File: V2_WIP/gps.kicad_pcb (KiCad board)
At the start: 6 copper layers, 82.5 x 82.5 mm, 126 parts, among them J301 USB_B_Micro, J601 BATT, P1 USB_C_Plug_USB2.0, Q1 IRLML5203, Q2 S8050, Q3 S8050, SW3 SW_Push, SW4 SW_Push, SW601 MSN22AFW01, SW701 RotaryEncoder, U1 ESP32-WROOM-32E, U10 24C32, U102 W25Q128JFV, U11 SN74LV1T34DBVRG4, U12 RT9742AGJ5F, U14 CH340K, U2 TPS613222ADBVR, U301 USBLC6-2SC6, U4 HT16k33, U401 NEO-M9N, U402 KW4-804CGB, U5 7seg_1x1_rgb, U6 7seg_1x1_rgb, U601 IP5306, U602 STC3100IST, U7 7seg_1x1_rgb, U9 TCA39306DDFR

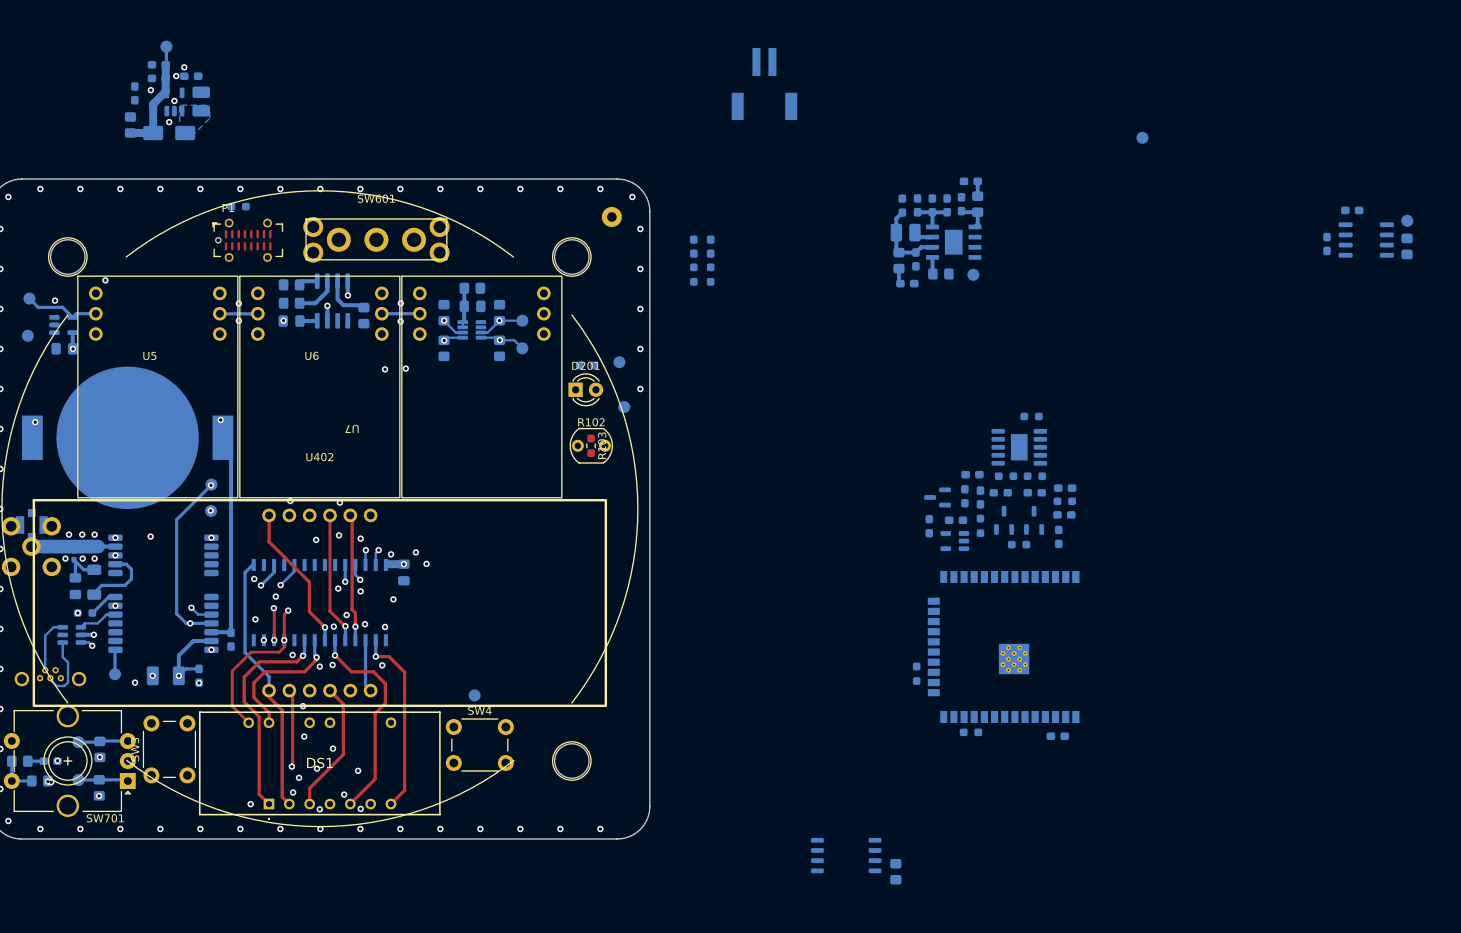
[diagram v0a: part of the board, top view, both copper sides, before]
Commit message: added USB, button
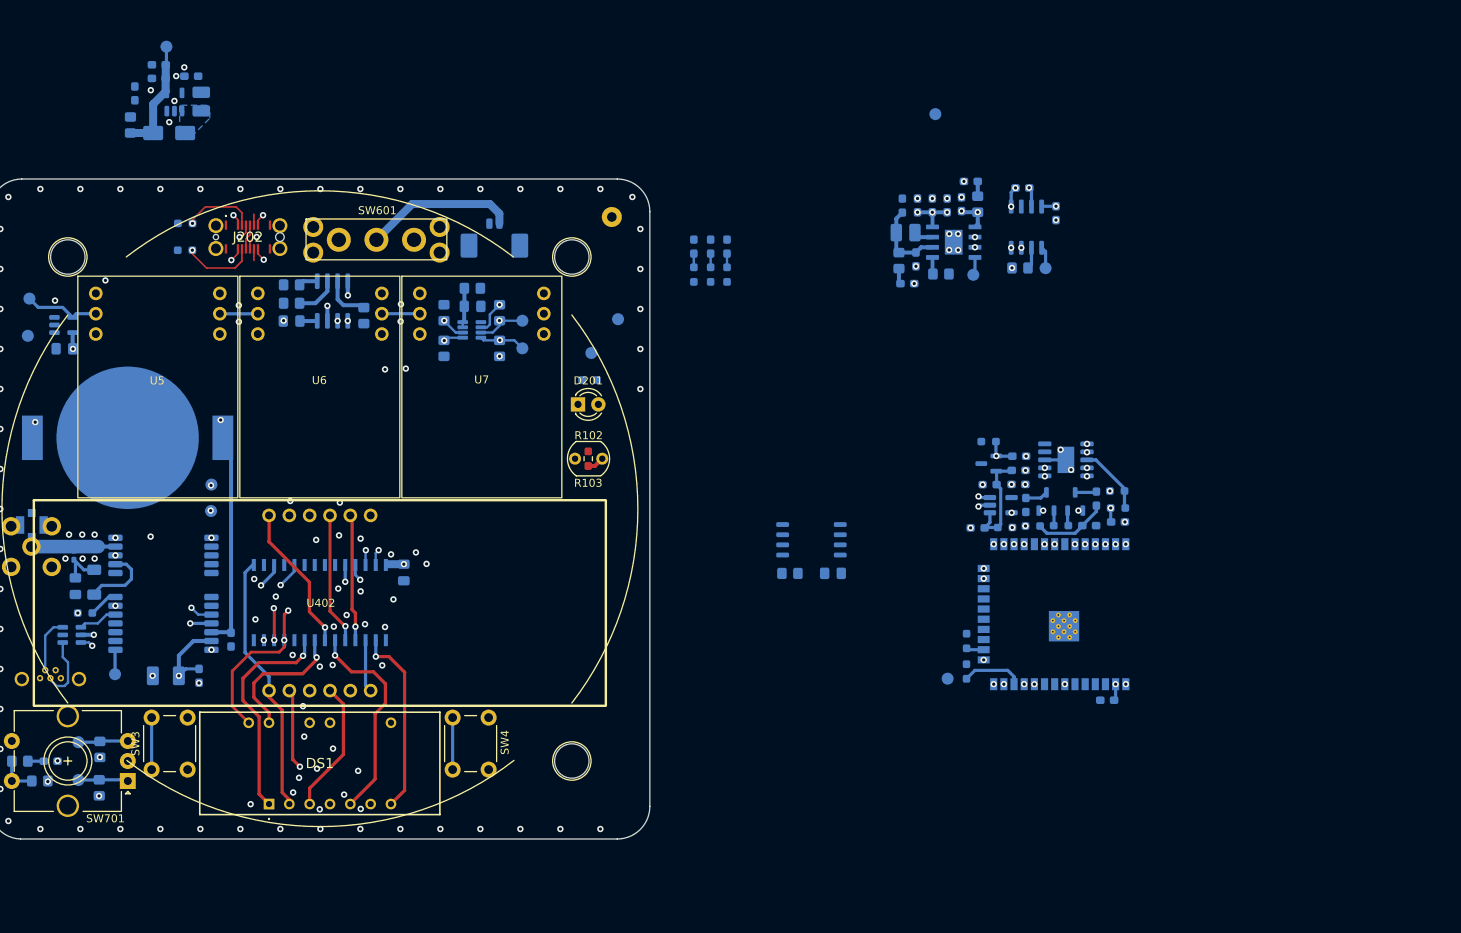
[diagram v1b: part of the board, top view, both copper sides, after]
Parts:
- removed D1: LED, Diode_SMD:D_0603_1608Metric_Pad1.05x0.95mm_HandSolder
- removed P1: USB_C_Plug_USB2.0, Connector_USB:USB_C_Receptacle_G-Switch_GT-USB-7051x
- removed R21: 5k1, Resistor_SMD:R_0603_1608Metric_Pad0.98x0.95mm_HandSolder
- removed U12: RT9742AGJ5F, Package_TO_SOT_SMD:TSOT-23-5
- added C101: 100nF, Capacitor_SMD:C_0805_2012Metric_Pad1.18x1.45mm_HandSolder, B.Cu at (158.1, 91.0)
- added D103: VUSB, Diode_SMD:D_0603_1608Metric_Pad1.05x0.95mm_HandSolder, B.Cu at (144.9, 50.2)
- added J202: USB4145-03-0230-C, KiCad:USB4145030230C, F.Cu at (85.0, 49.0)
- added R104: 2k, Resistor_SMD:R_0603_1608Metric_Pad0.98x0.95mm_HandSolder, B.Cu at (144.9, 53.7)
- added R204: 5k1, Resistor_SMD:R_0603_1608Metric_Pad0.98x0.95mm_HandSolder, B.Cu at (77.2, 47.3)
- added R205: 5k1, Resistor_SMD:R_0603_1608Metric_Pad0.98x0.95mm_HandSolder, B.Cu at (77.2, 50.6)
- added U201: RT9080, Package_TO_SOT_SMD:SOT-23-5_HandSoldering, B.Cu at (179.1, 82.5)
- D101: value LED -> +3V3
- D102: value LED -> +5V
- J601: footprint 1769:1769 -> Connector_Molex:Molex_PicoBlade_53398-0271_1x02-1MP_P1.25mm_Vertical
- SW3, SW4: value SW_Push -> FSM14JLH
- moved TP12 59.2 mm to (172.5, 104.2)
- moved R_E604 48.5 mm to (181.5, 52.9), turned to 0 degrees
- moved TP602 45.6 mm to (184.7, 52.9), turned to 90 degrees
- moved U602 42.5 mm to (182.3, 47.8), turned to 90 degrees
- moved J601 40.0 mm to (115.8, 48.6)
- moved U102 39.7 mm to (155.4, 86.8), turned to 0 degrees
- moved R_E102 39.6 mm to (152.8, 91.0), turned to 180 degrees
- moved C608 38.7 mm to (181.8, 42.9), turned to 180 degrees
- moved C609 37.0 mm to (186.0, 46.0), turned to -90 degrees
- moved C3 31.9 mm to (181.3, 79.9), turned to 0 degrees
- moved C2 29.4 mm to (192.4, 106.9)
- moved TP603 26.1 mm to (170.9, 33.6)
- moved R15 14.0 mm to (193.7, 80.8)
- moved R16 11.1 mm to (193.8, 82.9), turned to 0 degrees
- moved TP7 11.0 mm to (131.3, 59.3)
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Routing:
- net +3V3: track 101.8 -> 137.5 mm, vias 7 -> 11
- net /VUSB: track 17.4 -> 50.8 mm, vias 1 -> 11
- net /Display/SCL_5V: track 37.3 -> 56.8 mm, vias 2 -> 3
- net Net-(J601-Pin_1): track 0.00 -> 19.0 mm
- net /ESP/RST: track 0.00 -> 15.9 mm
- net /ESP/RTS: track 0.00 -> 15.6 mm, vias 0 -> 3
- net /ESP/VCC: track 0.00 -> 13.2 mm
- net /ESP/Rx: track 0.00 -> 11.6 mm, vias 0 -> 2
- net GND: track 3.66 -> 13.2 mm, vias 116 -> 141
- net Net-(J202-SBU2): track 0.00 -> 9.25 mm, vias 0 -> 1
- net Net-(J202-CC1): track 0.00 -> 9.17 mm, vias 0 -> 1
- net Net-(U14-V3): track 0.00 -> 8.98 mm, vias 0 -> 2
- net Net-(U14-TXD): track 0.00 -> 8.65 mm
- net Net-(U201-EN): track 0.00 -> 8.26 mm, vias 0 -> 2
- net /ESP/IO27/D4: track 0.00 -> 7.64 mm
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
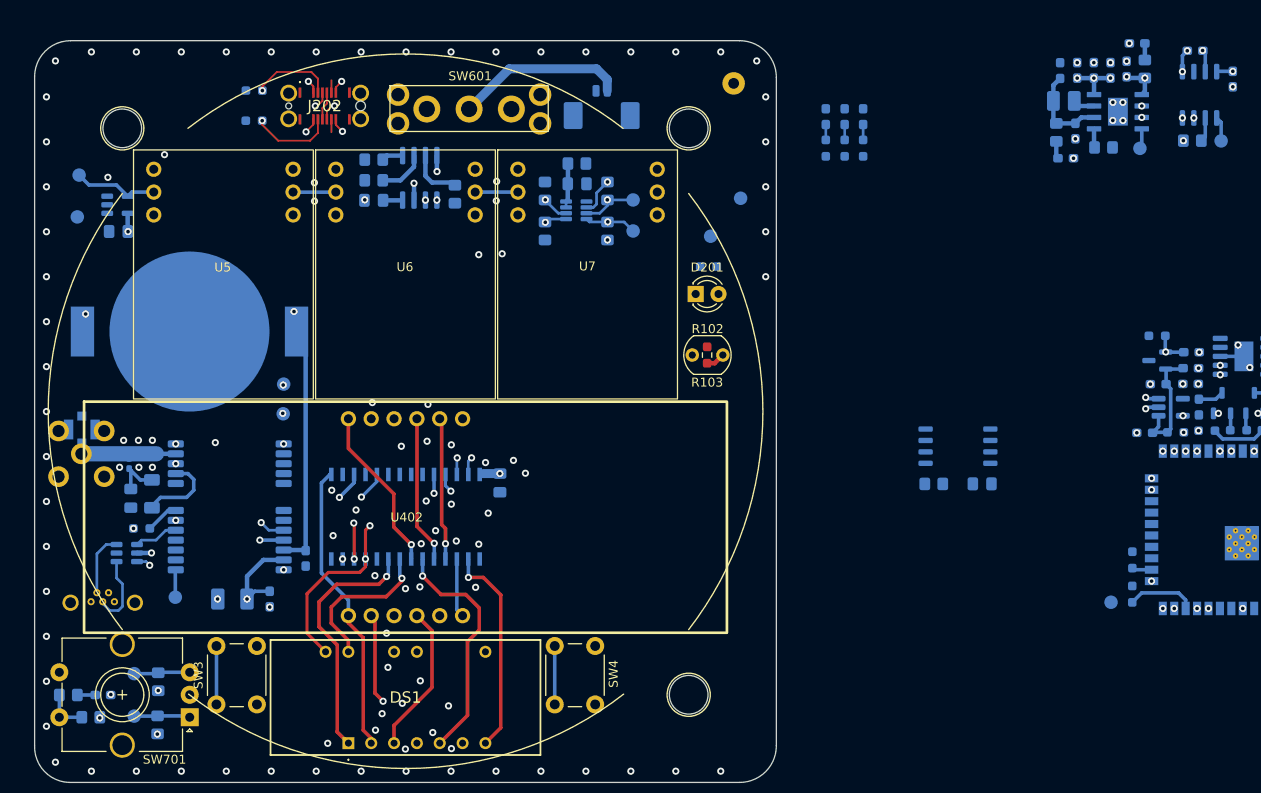
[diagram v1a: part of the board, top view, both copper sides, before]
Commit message: fixed errors in schematic
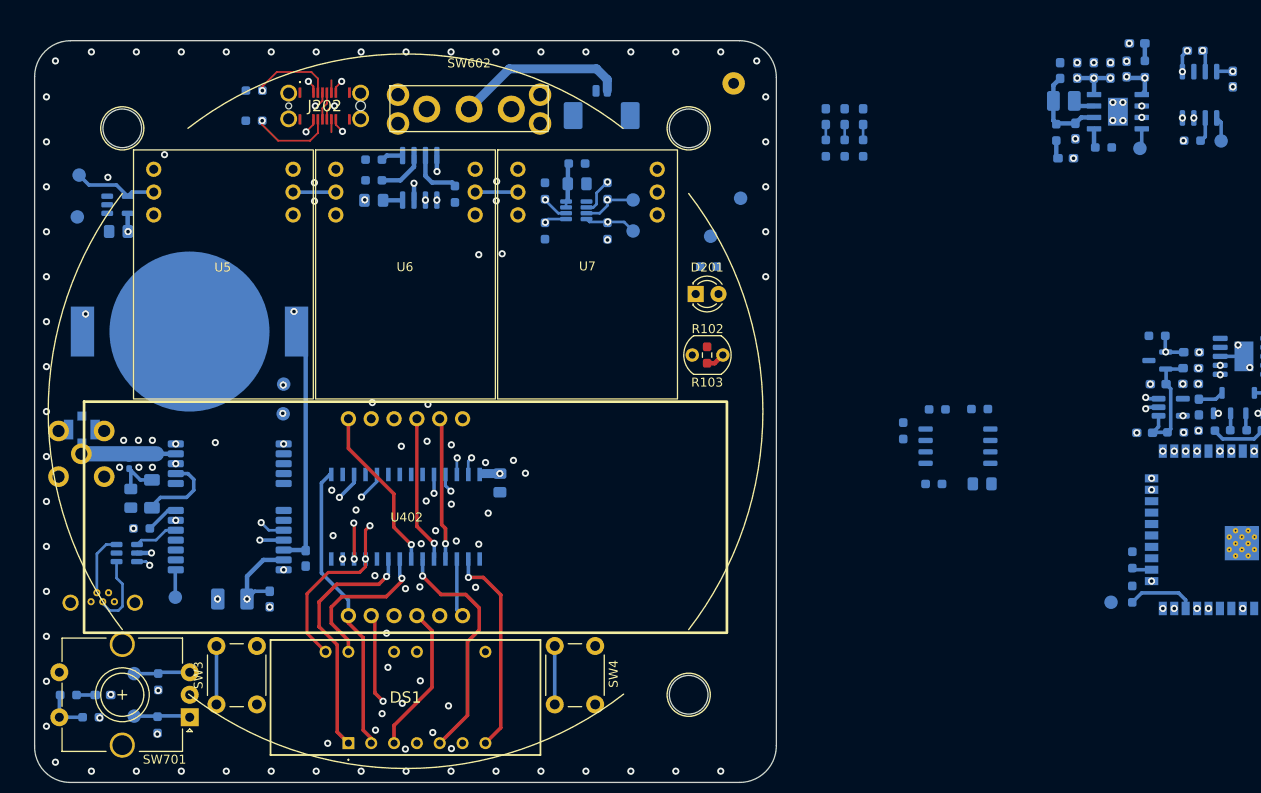
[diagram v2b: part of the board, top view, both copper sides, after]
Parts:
- removed SW601: MSN22AFW01, Button_Switch_THT:MSN22AFW01
- added R107: 0R, Resistor_SMD:R_0603_1608Metric_Pad0.98x0.95mm_HandSolder, B.Cu at (153.2, 82.8)
- added R108: 0R, Resistor_SMD:R_0603_1608Metric_Pad0.98x0.95mm_HandSolder, B.Cu at (149.4, 85.1)
- added R_E101: 10k, Resistor_SMD:R_0603_1608Metric_Pad0.98x0.95mm_HandSolder, B.Cu at (157.9, 82.7)
- added SW602: MSN22AFW01, Button_Switch_THT:MSN22AFW01, F.Cu at (101.1, 44.8)
- R17, R18, R19, RS1, R_E102, R_E601, R_E602, R_E603, R_E604, R_E701, R_E702, R_E703, R_E704: footprint Resistor_SMD:R_0805_2012Metric_Pad1.20x1.40mm_HandSolder -> Resistor_SMD:R_0603_1608Metric_Pad0.98x0.95mm_HandSolder
- R3, R4, R5, R6: value 4k7 -> 10k; footprint Resistor_SMD:R_0805_2012Metric_Pad1.20x1.40mm_HandSolder -> Resistor_SMD:R_0603_1608Metric_Pad0.98x0.95mm_HandSolder
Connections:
- net /Display/DPX renamed /Display/DP
- net /Display/L123 renamed /Display/CCL123
- net /Display/aBL2 renamed /Display/b
- net /Display/aCL3 renamed /Display/c
- net /Display/aD renamed /Display/d
- net /Display/aE renamed /Display/e
- net /Display/aF renamed /Display/f
- net /Display/aG renamed /Display/g
- net /ESP/IO0/D5 renamed /IO2
- net /ESP/IO12/D13 renamed /IO3
- net /ESP/IO13/D7 renamed /ESP/D7
- net /ESP/IO27/D4 renamed /ESP/D4
- net /ESP/IO2/D9 renamed /ESP/D9
- net /ESP/IO34/A2 renamed /ESP/A2
- net /ESP/IO36/A0 renamed /ESP/A0
- net /ESP/IO39/A1 renamed /ESP/A1
- U102 pad 7: Net-(U102-IO2) -> Net-(U102-IO3)
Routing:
- net GND: track 13.2 -> 70.7 mm, vias 141 -> 142
- net /Display/c: track 57.5 -> 0.00 mm, vias 1 -> 0

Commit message: schematic tweaks
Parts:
- U1: footprint RF_Module:ESP32-WROOM-32D -> RF_Module:ESP32-WROOM-32UE
- moved D101 83.0 mm to (90.6, 116.4), turned to 0 degrees
- moved C601 82.7 mm to (94.9, 68.3)
- moved C605 82.7 mm to (89.4, 68.5)
- moved R_E602 82.7 mm to (96.9, 68.3)
- moved R_E604 82.7 mm to (102.2, 76.3)
- moved U601 82.7 mm to (93.9, 73.1)
- moved C602 82.7 mm to (96.0, 65.5)
- moved C604 82.7 mm to (88.1, 78.2)
- moved C606 82.7 mm to (91.2, 68.5)
- moved C607 82.7 mm to (93.1, 68.5)
- moved C608 82.7 mm to (102.5, 66.3)
- moved C609 82.7 mm to (106.7, 69.4)
- moved D601 82.7 mm to (87.5, 68.5)
- moved L601 82.7 mm to (87.9, 71.9)
- moved C603 82.7 mm to (89.2, 75.2)
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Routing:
- net Net-(U102-IO3): track 0.00 -> 9.01 mm
- net Net-(U102-IO2): track 0.00 -> 8.39 mm
- net /ESP/VCC: track 13.2 -> 12.4 mm
- net +3V3: vias 11 -> 12
- net GND: vias 142 -> 144
- net /SCK: vias 1 -> 2
- net /MOSI: vias 1 -> 2
- net /MISO: vias 1 -> 2
- net /IO3: vias 1 -> 2
- net /IO2: vias 1 -> 2
- net /CS_N: vias 1 -> 2

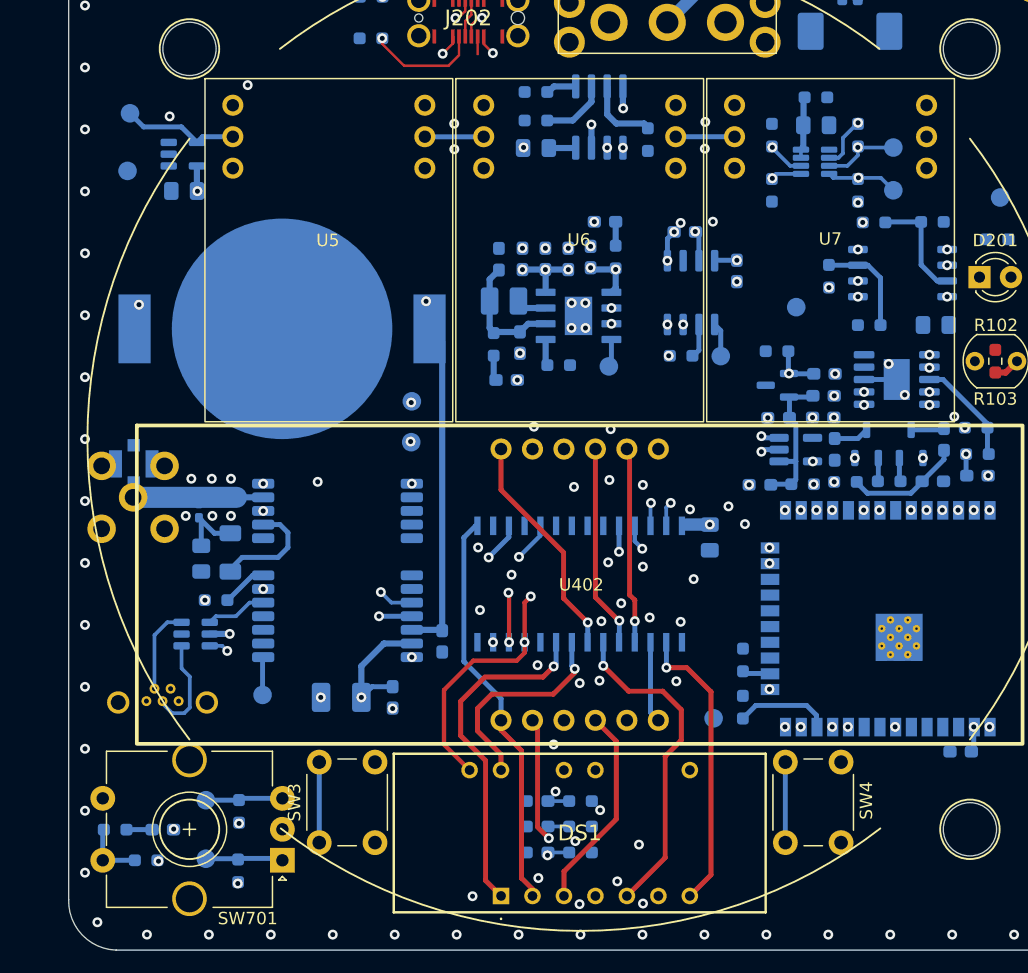
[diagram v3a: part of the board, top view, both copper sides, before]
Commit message: Removed EEPROM, Adjusted Flash connection, renamed ESP pins and several other signals
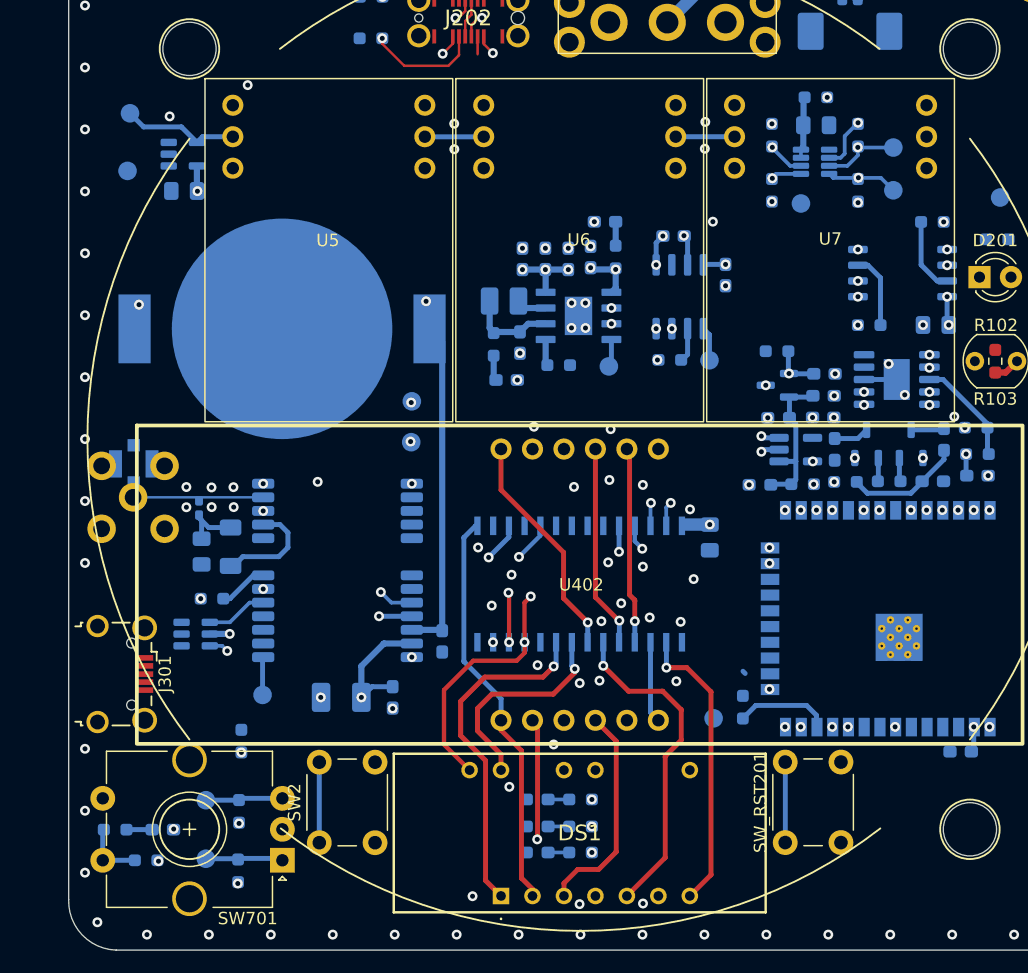
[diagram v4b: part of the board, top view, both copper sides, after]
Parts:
- removed C8: 100nF, Capacitor_SMD:C_0805_2012Metric_Pad1.18x1.45mm_HandSolder
- removed D601: D, Diode_SMD:D_0603_1608Metric_Pad1.05x0.95mm_HandSolder
- removed R105, R107, R108: 0R, Resistor_SMD:R_0603_1608Metric_Pad0.98x0.95mm_HandSolder
- removed R17, R18, R19: 4k7, Resistor_SMD:R_0603_1608Metric_Pad0.98x0.95mm_HandSolder
- removed SW3, SW4: FSM14JLH, Button_Switch_THT:SW_PUSH_6mm
- removed U10: 24C32, Package_SO:SOIC-8_3.9x4.9mm_P1.27mm
- added R302: 0R, Resistor_SMD:R_0603_1608Metric_Pad0.98x0.95mm_HandSolder, B.Cu at (66.7, 107.4)
- added SW2: FSM14JLH, Button_Switch_THT:SW_PUSH_6mm, F.Cu at (73.0, 115.6)
- added SW_RST201: FSM14JLH, Button_Switch_THT:SW_PUSH_6mm, F.Cu at (110.6, 115.6)
- J301: footprint KiCad:USB3145301A -> Connector_USB:USB_Micro-B_Wuerth_629105150521_CircularHoles; moved to F.Cu
- moved TP603 8.38 mm to (111.9, 64.0)
- moved D103 4.15 mm to (90.6, 116.4)
- moved R104 4.15 mm to (94.1, 116.4)
- moved J301 3.84 mm to (57.0, 102.0), turned to -90 degrees
- moved D102 2.18 mm to (90.6, 112.1)
- moved R106 2.18 mm to (94.1, 112.1)
- moved D101 2.10 mm to (90.6, 114.3)
- moved R101 2.10 mm to (94.1, 114.3)
- moved TP602 0.97 mm to (104.5, 76.6)
- moved C609 0.97 mm to (105.8, 69.8)
- moved U602 0.97 mm to (102.1, 71.5)
- moved C608 0.97 mm to (101.6, 66.6)
- moved R_E604 0.97 mm to (101.3, 76.6)
- moved C403 0.57 mm to (63.5, 92.1)
- moved R401 0.46 mm to (65.8, 91.7)
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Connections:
- net /ESP/A0 renamed /ESP/SENSOR_VP
- net /ESP/A1 renamed /ESP/SENSOR_VN
- net /ESP/A2 renamed /ESP/IO34
- net /ESP/D4 renamed /ESP/IO27
- net /ESP/D9 renamed /ESP/IO2
- net /ESP/Rx renamed /ESP/RXD0
- net /ESP/Tx renamed /ESP/TXD0
- net /IO2 renamed /ESP/IO0
- net /IO3 renamed /ESP/IO12
- J301 pad 1: /VUSB -> Net-(J301-VBUS)
- U1 pad 16: /ESP/D7 -> /ESP/IO13
- U301 pad 5: /VUSB -> Net-(J301-VBUS)
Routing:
- net +3V3: track 137.5 -> 25.3 mm, vias 12 -> 16
- net GND: track 70.7 -> 9.51 mm, vias 144 -> 130
- net /Display/c: track 0.00 -> 58.2 mm, vias 0 -> 1
- net +5V: track 14.3 -> 62.8 mm, vias 6 -> 10
- net /VUSB: track 50.8 -> 91.9 mm, vias 11 -> 12
- net /Display/SCL_5V: track 56.8 -> 38.6 mm, vias 3 -> 2
- net /Display/SDA_5V: track 45.9 -> 34.2 mm, vias 3 -> 2
- net Net-(J301-D+): track 8.17 -> 0.00 mm
- net Net-(J301-D-): track 6.94 -> 0.00 mm
- net Net-(U10-E2): track 5.97 -> 0.00 mm
- net Net-(U10-E1): track 5.35 -> 0.00 mm
- net Net-(U102-IO3): track 9.01 -> 6.10 mm
- net Net-(D601-K): track 9.92 -> 7.11 mm
- net Net-(U10-E0): track 2.40 -> 0.00 mm
- net Net-(U102-IO2): track 8.39 -> 6.06 mm
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- added copper zone on In2.Cu, net +3V3
- added copper zone on In2.Cu, net /VUSB
